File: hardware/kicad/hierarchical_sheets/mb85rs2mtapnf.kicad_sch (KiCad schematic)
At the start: 0 parts

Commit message: Fixed
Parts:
- added C6: 100nF, symbol Device:C
- added R2: 1k, symbol Device:R
- added U5: MB85RS2, symbol Memory_NVRAM:MB85RS16
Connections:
- new net: R2.1, U5.1 (~{CS})
- new net +3.3V: C6.1, U5.8 (VDD)
- new net GND: C6.2, U5.4 (GND)
- new net SCK: U5.6 (SCK)
- new net SI: U5.5 (SI)
- new net SO: U5.2 (SO)
- new net ~{CS}: R2.2
- new net ~{HOLD}: U5.7 (~{HOLD})
- no-connect marks 0 -> 1
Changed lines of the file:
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@@
     (company "Missouri S&T Rocket Design Team")
   )
+  (junction (at 49.53 27.94) (diameter 0) (color 0 0 0 0)
+  )
+  (junction (at 49.53 55.88) (diameter 0) (color 0 0 0 0)
+  )
+  (no_connect (at 39.37 38.1))
+  (wire (pts (xy 34.29 50.8) (xy 35.56 50.8))
+    (stroke (width 0) (type default))
+  )
+  (wire (pts (xy 49.53 27.94) (xy 49.53 33.02))
+    (stroke (width 0) (type default))
+  )
+  (wire (pts (xy 49.53 55.88) (xy 49.53 48.26))
+    (stroke (width 0) (type default))
+  )
+  (wire (pts (xy 71.12 38.1) (xy 59.69 38.1))
+    (stroke (width 0) (type default))
+  )
+  (wire (pts (xy 85.09 55.88) (xy 49.53 55.88))
+    (stroke (width 0) (type default))
+  )
+  (wire (pts (xy 85.09 36.83) (xy 85.09 27.94))
+    (stroke (width 0) (type default))
+  )
+  (wire (pts (xy 85.09 44.45) (xy 85.09 55.88))
+    (stroke (width 0) (type default))
+  )
+  (wire (pts (xy 49.53 26.67) (xy 49.53 27.94))
+    (stroke (width 0) (type default))
+  )
+  (wire (pts (xy 49.53 57.15) (xy 49.53 55.88))
+    (stroke (width 0) (type default))
+  )
+  (wire (pts (xy 59.69 40.64) (xy 71.12 40.64))
+    (stroke (width 0) (type default))
+  )
+  (wire (pts (xy 85.09 27.94) (xy 49.53 27.94))
+    (stroke (width 0) (type default))
+  )
+  (wire (pts (xy 35.56 43.18) (xy 39.37 43.18))
+    (stroke (width 0) (type default))
+  )
+  (wire (pts (xy 59.69 43.18) (xy 71.12 43.18))
+    (stroke (width 0) (type default))
+  )
+  (wire (pts (xy 30.48 40.64) (xy 39.37 40.64))
+    (stroke (width 0) (type default))
+  )
+  (hierarchical_label "~{HOLD}" (shape input) (at 30.48 40.64 180) (fields_autoplaced)
+    (effects (font (size 1.27 1.27)) (justify right))
+  )
+  (hierarchical_label "~{CS}" (shape input) (at 34.29 50.8 180) (fields_autoplaced)
+    (effects (font (size 1.27 1.27)) (justify right))
+  )
+  (hierarchical_label "SO" (shape output) (at 71.12 43.18 0) (fields_autoplaced)
+    (effects (font (size 1.27 1.27)) (justify left))
+  )
+  (hierarchical_label "SCK" (shape input) (at 71.12 38.1 0) (fields_autoplaced)
+    (effects (font (size 1.27 1.27)) (justify left))
+  )
+  (hierarchical_label "SI" (shape input) (at 71.12 40.64 0) (fields_autoplaced)
+    (effects (font (size 1.27 1.27)) (justify left))
+  )
+  (symbol (lib_id "Device:R") (at 35.56 46.99 0) (unit 1)
+    (in_bom yes) (on_board yes) (dnp no) (fields_autoplaced)
+    (property "Reference" "R2" (at 38.1 45.72 0)
+      (effects (font (size 1.27 1.27)) (justify left))
+    )
+    (property "Value" "1k" (at 38.1 48.26 0)
+      (effects (font (size 1.27 1.27)) (justify left))
+    )
+    (property "Footprint" "" (at 33.782 46.99 90)
+      (effects (font (size 1.27 1.27)) hide)
+    )
+    (property "Datasheet" "~" (at 35.56 46.99 0)
+      (effects (font (size 1.27 1.27)) hide)
+    )
+    (pin "1")
+    (pin "2")
+    (instances
+      (project "FC"
+        (path "/54cce219-8b98-4e71-96c4-f9ee784aa3bc/ec693876-f9f5-4d00-b73f-be61605a2d0a"
+          (reference "R2") (unit 1)
+        )
+      )
+    )
+  )
+  (symbol (lib_id "power:GND") (at 49.53 57.15 0) (unit 1)
+    (in_bom yes) (on_board yes) (dnp no) (fields_autoplaced)
+    (property "Reference" "#PWR05" (at 49.53 63.5 0)
+      (effects (font (size 1.27 1.27)) hide)
+    )
+    (property "Value" "GND" (at 49.53 62.23 0)
+      (effects (font (size 1.27 1.27)))
+    )
+    (property "Footprint" "" (at 49.53 57.15 0)
+      (effects (font (size 1.27 1.27)) hide)
+    )
+    (property "Datasheet" "" (at 49.53 57.15 0)
+      (effects (font (size 1.27 1.27)) hide)
+    )
+    (pin "1")
+    (instances
+      (project "FC"
+        (path "/54cce219-8b98-4e71-96c4-f9ee784aa3bc/ec693876-f9f5-4d00-b73f-be61605a2d0a"
+          (reference "#PWR05") (unit 1)
+        )
+      )
+    )
+  )
+  (symbol (lib_id "power:+3.3V") (at 49.53 26.67 0) (unit 1)
+    (in_bom yes) (on_board yes) (dnp no)
+    (property "Reference" "#PWR07" (at 49.53 30.48 0)
+      (effects (font (size 1.27 1.27)) hide)
+    )
+    (property "Value" "+3.3V" (at 49.53 21.59 0)
+      (effects (font (size 1.27 1.27)))
+    )
+    (property "Footprint" "" (at 49.53 26.67 0)
+      (effects (font (size 1.27 1.27)) hide)
+    )
+    (property "Datasheet" "" (at 49.53 26.67 0)
+      (effects (font (size 1.27 1.27)) hide)
+    )
+    (pin "1")
+    (instances
+      (project "FC"
+        (path "/54cce219-8b98-4e71-96c4-f9ee784aa3bc/ec693876-f9f5-4d00-b73f-be61605a2d0a"
+          (reference "#PWR07") (unit 1)
+        )
+      )
+    )
+  )
+  (symbol (lib_id "Device:C") (at 85.09 40.64 0) (unit 1)
+    (in_bom yes) (on_board yes) (dnp no) (fields_autoplaced)
+    (property "Reference" "C6" (at 88.9 39.37 0)
+      (effects (font (size 1.27 1.27)) (justify left))
+    )
+    (property "Value" "100nF" (at 88.9 41.91 0)
+      (effects (font (size 1.27 1.27)) (justify left))
+    )
+    (property "Footprint" "" (at 86.0552 44.45 0)
+      (effects (font (size 1.27 1.27)) hide)
+    )
+    (property "Datasheet" "~" (at 85.09 40.64 0)
+      (effects (font (size 1.27 1.27)) hide)
+    )
+    (pin "1")
+    (pin "2")
+    (instances
+      (project "FC"
+        (path "/54cce219-8b98-4e71-96c4-f9ee784aa3bc/ec693876-f9f5-4d00-b73f-be61605a2d0a"
+          (reference "C6") (unit 1)
+        )
+      )
+    )
+  )
+  (symbol (lib_id "Memory_NVRAM:MB85RS16") (at 49.53 40.64 0) (unit 1)
+    (in_bom yes) (on_board yes) (dnp no) (fields_autoplaced)
+    (property "Reference" "U5" (at 51.7241 30.48 0)
+      (effects (font (size 1.27 1.27)) (justify left))
+    )
+    (property "Value" "MB85RS2" (at 51.7241 33.02 0)
+      (effects (font (size 1.27 1.27)) (justify left))
+    )
+    (property "Footprint" "" (at 40.64 41.91 0)
+      (effects (font (size 1.27 1.27)) hide)
+    )
+    (property "Datasheet" "http://www.fujitsu.com/downloads/MICRO/fsa/pdf/products/memory/fram/MB85RS16-DS501-00014-6v0-E.pdf" (at 40.64 41.91 0)
+      (effects (font (size 1.27 1.27)) hide)
+    )
+    (pin "1")
+    (pin "2")
+    (pin "3")
+    (pin "4")
+    (pin "5")
+    (pin "6")
+    (pin "7")
+    (pin "8")
+    (instances
+      (project "FC"
+        (path "/54cce219-8b98-4e71-96c4-f9ee784aa3bc/ec693876-f9f5-4d00-b73f-be61605a2d0a"
+          (reference "U5") (unit 1)
+        )
+      )
+    )
+  )
 )

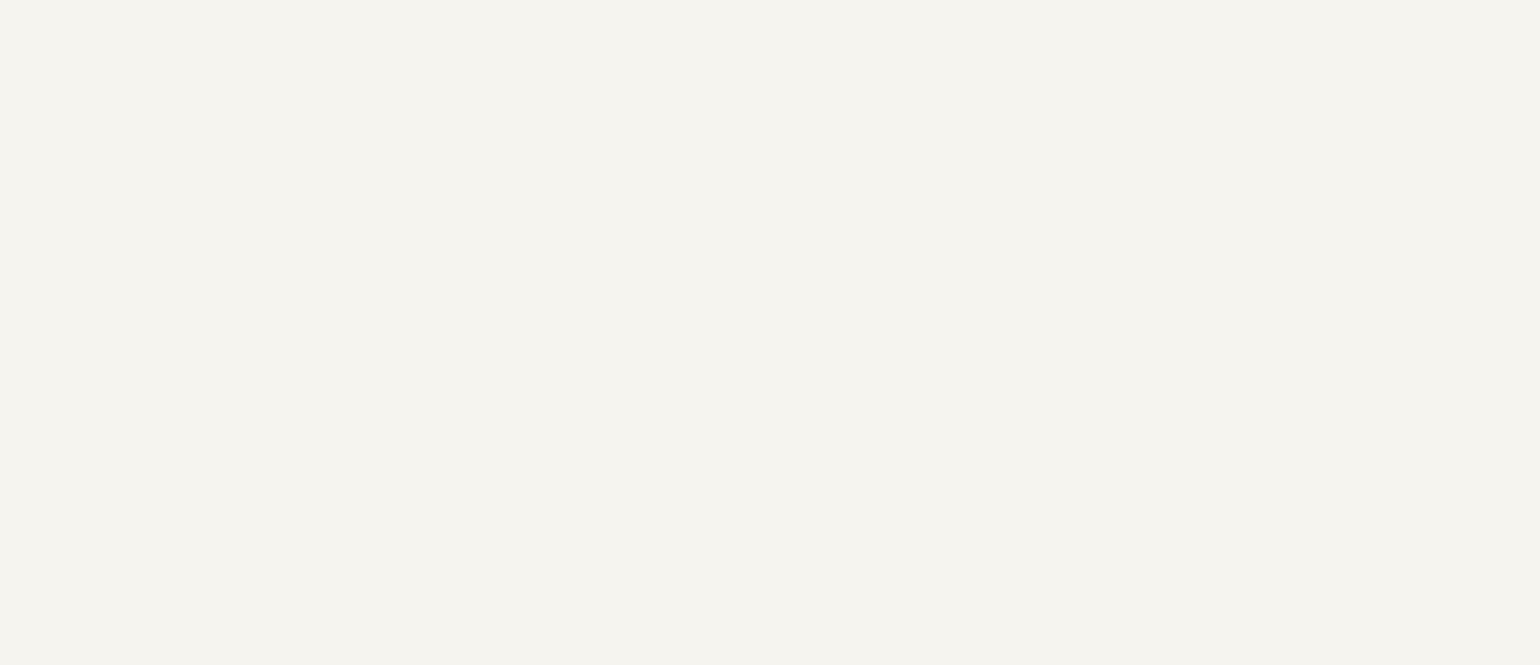
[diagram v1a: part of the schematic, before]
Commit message: added comments to storage and telemetry radio
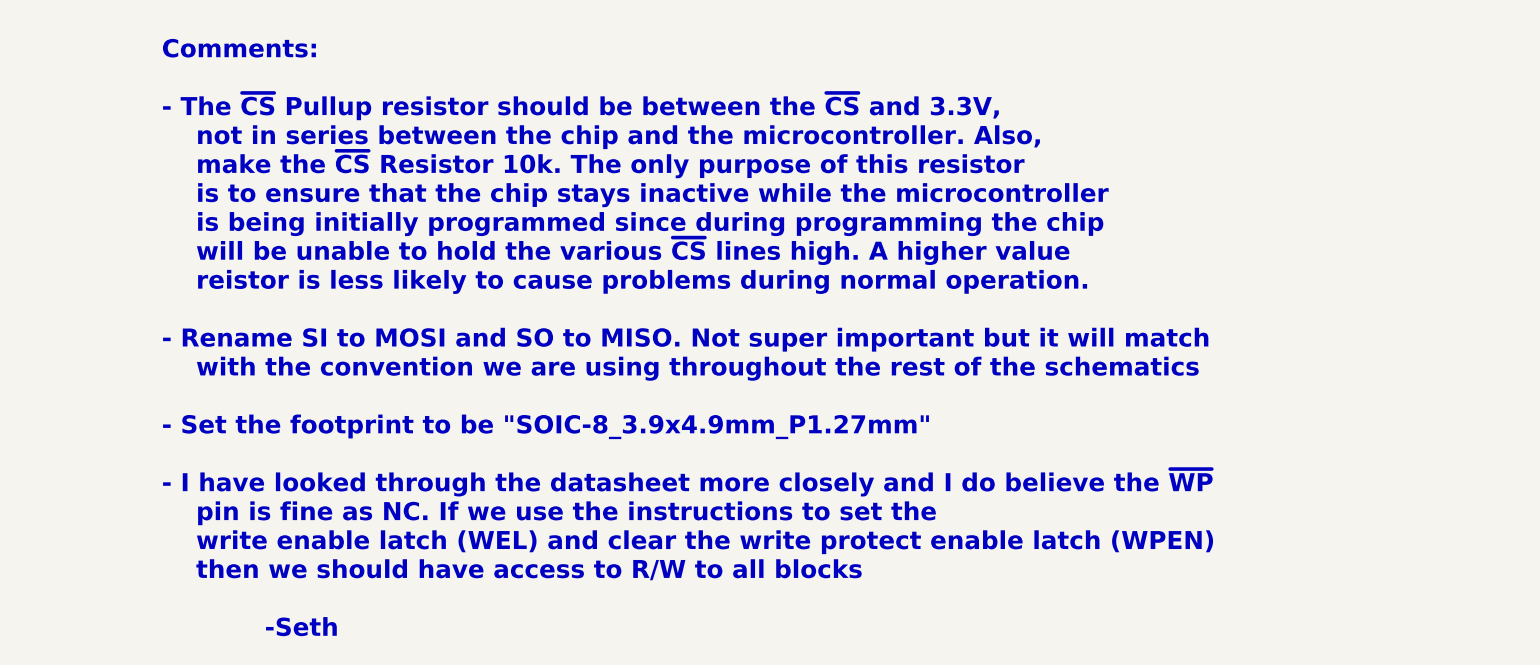
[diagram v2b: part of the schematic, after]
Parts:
- U5: Digikey (none) -> https://www.digikey.com/en/products/detail/kaga-fei-america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
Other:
- note added: "Comments: - The ~{CS} Pullup resistor should be between the ~{CS} and 3.3V, not in series between the chip and the microcontroller. Also, make the ~{CS} Resistor 10k. The only purpose of this resistor is to ensure that the chip stays inactive while the microcontroller is being initially programmed since during programming the chip will be unable to hold the various ~{CS} lines high. A higher valu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"

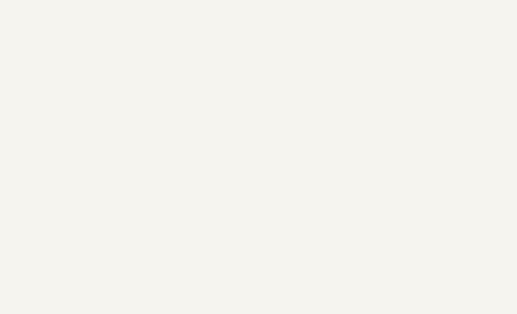
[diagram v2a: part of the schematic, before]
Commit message: added max current
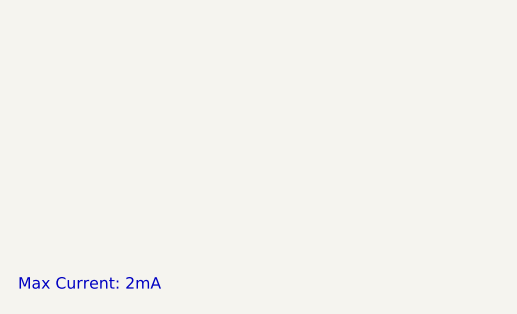
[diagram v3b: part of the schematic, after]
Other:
- note added: "Max Current: 2mA"
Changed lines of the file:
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@@
     )
+  )
+  (text "Max Current: 2mA" (at 13.97 201.93 0)
+    (effects (font (size 1.27 1.27)) (justify left bottom))
   )
   (text "Comments:\n\n- The ~{CS} Pullup resistor should be between the ~{CS} and 3.3V, \n	not in series between the chip and the microcontroller. Also, \n	make the ~{CS} Resistor 10k. The only purpose of this resistor\n	is to ensure that the chip stays inactive while the microcontroller\n	is being initially programmed since during programming the chip\n	will be unable to hold the various ~{CS} lines high. A higher value \n	reistor is less likely to cause problems during normal operation. \n\n- Rename SI to MOSI and SO to MISO. Not super important but it will match\n	with the convention we are using throughout the rest of the schematics\n\n- Set the footprint to be \"SOIC-8_3.9x4.9mm_P1.27mm\"\n\n- I have looked through the datasheet more closely and I do believe the ~{WP}\n	pin is fine as NC. If we use the instructions to set the \n	write enable latch (WEL) and clear the write protect enable latch (WPEN)\n	then we should have access to R/W to all blocks \n\n			-Seth"

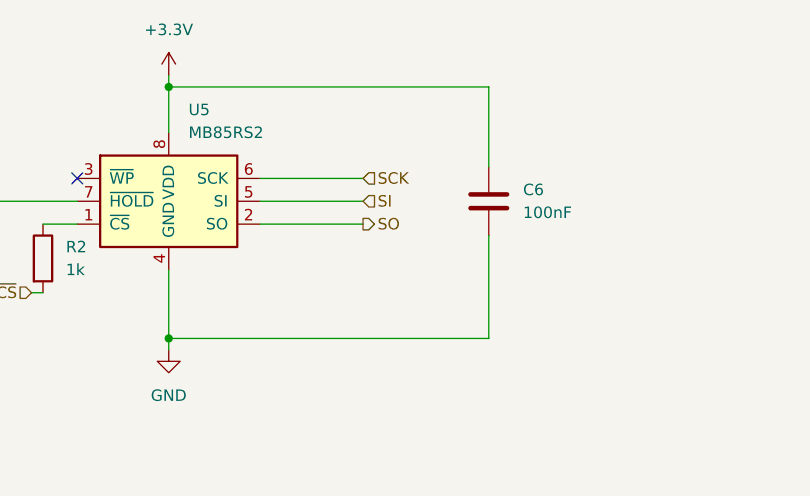
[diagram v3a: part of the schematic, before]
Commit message: changed FRAM labels
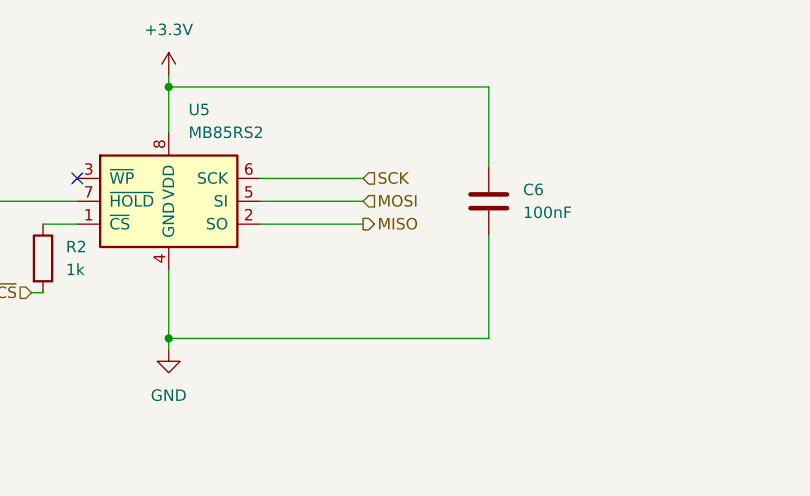
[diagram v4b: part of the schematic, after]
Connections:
- net SI renamed MOSI
- net SO renamed MISO
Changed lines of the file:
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@@
     (effects (font (size 1.27 1.27)) (justify right))
   )
-  (hierarchical_label "SO" (shape output) (at 71.12 43.18 0) (fields_autoplaced)
+  (hierarchical_label "MISO" (shape output) (at 71.12 43.18 0) (fields_autoplaced)
     (effects (font (size 1.27 1.27)) (justify left))
   )
@@
     (effects (font (size 1.27 1.27)) (justify left))
   )
-  (hierarchical_label "SI" (shape input) (at 71.12 40.64 0) (fields_autoplaced)
+  (hierarchical_label "MOSI" (shape input) (at 71.12 40.64 0) (fields_autoplaced)
     (effects (font (size 1.27 1.27)) (justify left))
   )

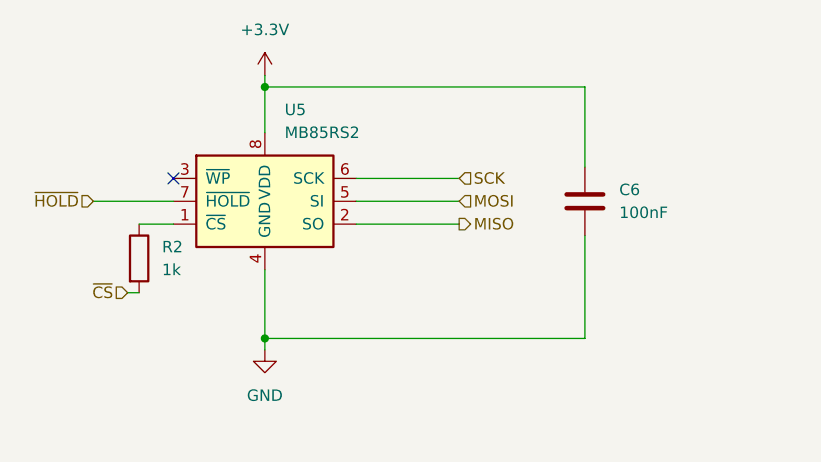
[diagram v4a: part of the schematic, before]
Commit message: assigned footprints
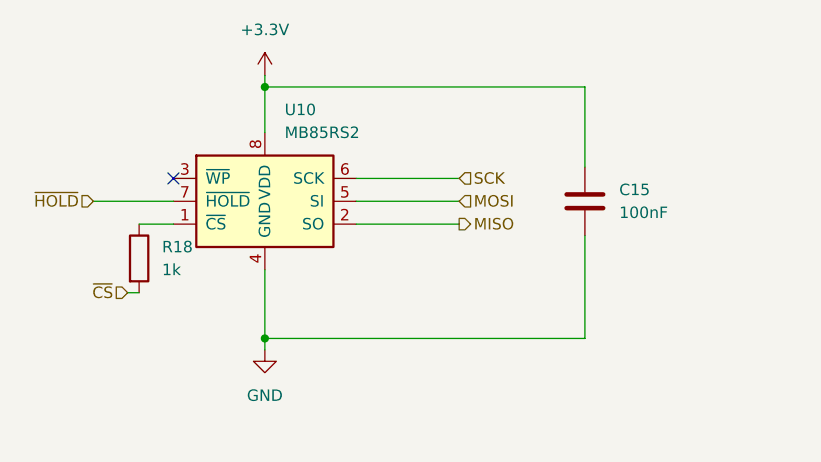
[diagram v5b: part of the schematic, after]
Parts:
- C15: renamed from C6; footprint (none) -> Resistor_SMD:R_0603_1608Metric
- R18: renamed from R2; footprint (none) -> Resistor_SMD:R_0603_1608Metric
- renumbered U5 to U10
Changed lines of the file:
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@@
   (symbol (lib_id "Device:R") (at 35.56 46.99 0) (unit 1)
     (in_bom yes) (on_board yes) (dnp no) (fields_autoplaced)
-    (property "Reference" "R2" (at 38.1 45.72 0)
+    (property "Reference" "R18" (at 38.1 45.72 0)
       (effects (font (size 1.27 1.27)) (justify left))
     )
@@
       (effects (font (size 1.27 1.27)) (justify left))
     )
-    (property "Footprint" "" (at 33.782 46.99 90)
+    (property "Footprint" "Resistor_SMD:R_0603_1608Metric" (at 33.782 46.99 90)
       (effects (font (size 1.27 1.27)) hide)
     )
@@
       (project "FC"
         (path "/54cce219-8b98-4e71-96c4-f9ee784aa3bc/ec693876-f9f5-4d00-b73f-be61605a2d0a"
-          (reference "R2") (unit 1)
+          (reference "R18") (unit 1)
         )
       )
@@
   (symbol (lib_id "power:GND") (at 49.53 57.15 0) (unit 1)
     (in_bom yes) (on_board yes) (dnp no) (fields_autoplaced)
-    (property "Reference" "#PWR05" (at 49.53 63.5 0)
+    (property "Reference" "#PWR043" (at 49.53 63.5 0)
       (effects (font (size 1.27 1.27)) hide)
     )
@@
       (project "FC"
         (path "/54cce219-8b98-4e71-96c4-f9ee784aa3bc/ec693876-f9f5-4d00-b73f-be61605a2d0a"
-          (reference "#PWR05") (unit 1)
+          (reference "#PWR043") (unit 1)
         )
       )
@@
   (symbol (lib_id "power:+3.3V") (at 49.53 26.67 0) (unit 1)
     (in_bom yes) (on_board yes) (dnp no)
-    (property "Reference" "#PWR07" (at 49.53 30.48 0)
+    (property "Reference" "#PWR042" (at 49.53 30.48 0)
       (effects (font (size 1.27 1.27)) hide)
     )
@@
       (project "FC"
         (path "/54cce219-8b98-4e71-96c4-f9ee784aa3bc/ec693876-f9f5-4d00-b73f-be61605a2d0a"
-          (reference "#PWR07") (unit 1)
+          (reference "#PWR042") (unit 1)
         )
       )
@@
   (symbol (lib_id "Device:C") (at 85.09 40.64 0) (unit 1)
     (in_bom yes) (on_board yes) (dnp no) (fields_autoplaced)
-    (property "Reference" "C6" (at 88.9 39.37 0)
+    (property "Reference" "C15" (at 88.9 39.37 0)
       (effects (font (size 1.27 1.27)) (justify left))
     )
@@
       (effects (font (size 1.27 1.27)) (justify left))
     )
-    (property "Footprint" "" (at 86.0552 44.45 0)
+    (property "Footprint" "Resistor_SMD:R_0603_1608Metric" (at 86.0552 44.45 0)
       (effects (font (size 1.27 1.27)) hide)
     )
@@
       (project "FC"
         (path "/54cce219-8b98-4e71-96c4-f9ee784aa3bc/ec693876-f9f5-4d00-b73f-be61605a2d0a"
-          (reference "C6") (unit 1)
+          (reference "C15") (unit 1)
         )
       )
@@
   (symbol (lib_id "Memory_NVRAM:MB85RS16") (at 49.53 40.64 0) (unit 1)
     (in_bom yes) (on_board yes) (dnp no) (fields_autoplaced)
-    (property "Reference" "U5" (at 51.7241 30.48 0)
+    (property "Reference" "U10" (at 51.7241 30.48 0)
       (effects (font (size 1.27 1.27)) (justify left))
     )
@@
       (project "FC"
         (path "/54cce219-8b98-4e71-96c4-f9ee784aa3bc/ec693876-f9f5-4d00-b73f-be61605a2d0a"
-          (reference "U5") (unit 1)
+          (reference "U10") (unit 1)
         )
       )
